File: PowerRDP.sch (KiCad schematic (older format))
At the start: 40 parts, among them J1 Conn_01x02_Male, J10 FPGA, J11 FAA LED, J12 Switch, J2 Conn_01x02_Male, J3 Conn_01x02_Male, J4 Conn_01x02_Male, J5 Conn_01x02_Male, J6 Conn_01x02_Male, J7 3.3V, J8 5V, J9 12V, Q1 NTR4003NT1G, U1 Recom_RS3, U2 LM2575-3.3BU, U3 LM2575-5.0BU, U4 LM2575-12BU, U5 TS555

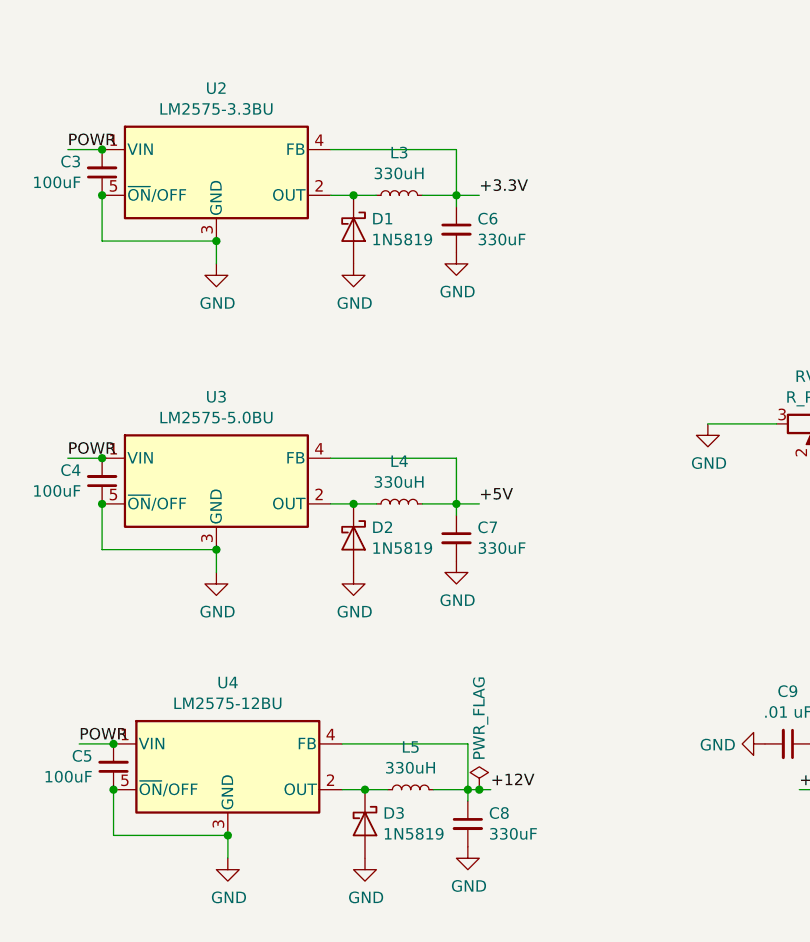
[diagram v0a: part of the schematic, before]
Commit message: Fix capcaitors and inductors and expand board to sustain girth of new components.
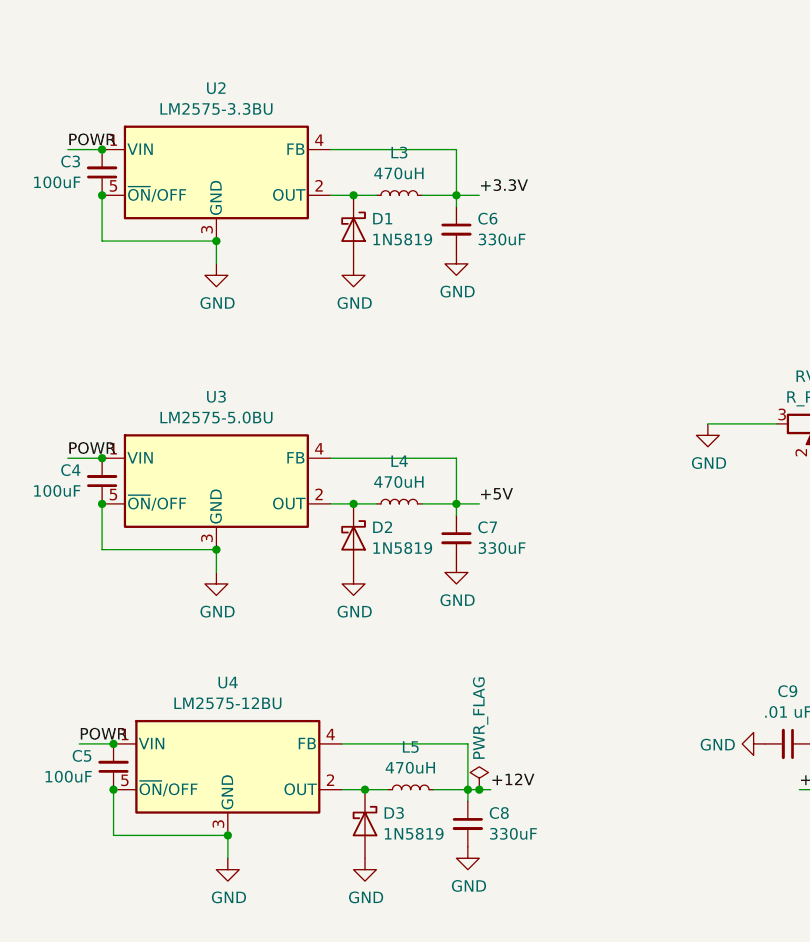
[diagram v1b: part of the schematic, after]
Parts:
- C3, C4, C5: footprint Capacitor_SMD:C_0805_2012Metric_Pad1.15x1.40mm_HandSolder -> Capacitor_SMD:CP_Elec_6.3x7.7
- C6, C7, C8: footprint Capacitor_SMD:C_0805_2012Metric_Pad1.15x1.40mm_HandSolder -> Capacitor_SMD:CP_Elec_8x10
- L3, L4, L5: value 330uH -> 470uH; footprint Inductor_SMD:L_0805_2012Metric_Pad1.15x1.40mm_HandSolder -> Inductor_SMD:L_Bourns_SRR1260
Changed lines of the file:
@@
 P 6850 1350
 F 0 "L3" V 7035 1350 50  0000 C CNN
-F 1 "330uH" V 6944 1350 50  0000 C CNN
-F 2 "Inductor_SMD:L_0805_2012Metric_Pad1.15x1.40mm_HandSolder" H 6850 1350 50  0001 C CNN
+F 1 "470uH" V 6944 1350 50  0000 C CNN
+F 2 "Inductor_SMD:L_Bourns_SRR1260" H 6850 1350 50  0001 C CNN
 F 3 "~" H 6850 1350 50  0001 C CNN
 	1    6850 1350
@@
 F 0 "C6" H 7192 1546 50  0000 L CNN
 F 1 "330uF" H 7192 1455 50  0000 L CNN
-F 2 "Capacitor_SMD:C_0805_2012Metric_Pad1.15x1.40mm_HandSolder" H 7100 1500 50  0001 C CNN
+F 2 "Capacitor_SMD:CP_Elec_8x10" H 7100 1500 50  0001 C CNN
 F 3 "~" H 7100 1500 50  0001 C CNN
 	1    7100 1500
@@
 F 0 "C4" H 5459 2554 50  0000 R CNN
 F 1 "100uF" H 5459 2645 50  0000 R CNN
-F 2 "Capacitor_SMD:C_0805_2012Metric_Pad1.15x1.40mm_HandSolder" H 5550 2600 50  0001 C CNN
+F 2 "Capacitor_SMD:CP_Elec_6.3x7.7" H 5550 2600 50  0001 C CNN
 F 3 "~" H 5550 2600 50  0001 C CNN
 	1    5550 2600
@@
 P 6850 2700
 F 0 "L4" V 7035 2700 50  0000 C CNN
-F 1 "330uH" V 6944 2700 50  0000 C CNN
-F 2 "Inductor_SMD:L_0805_2012Metric_Pad1.15x1.40mm_HandSolder" H 6850 2700 50  0001 C CNN
+F 1 "470uH" V 6944 2700 50  0000 C CNN
+F 2 "Inductor_SMD:L_Bourns_SRR1260" H 6850 2700 50  0001 C CNN
 F 3 "~" H 6850 2700 50  0001 C CNN
 	1    6850 2700
@@
 F 0 "C7" H 7192 2896 50  0000 L CNN
 F 1 "330uF" H 7192 2805 50  0000 L CNN
-F 2 "Capacitor_SMD:C_0805_2012Metric_Pad1.15x1.40mm_HandSolder" H 7100 2850 50  0001 C CNN
+F 2 "Capacitor_SMD:CP_Elec_8x10" H 7100 2850 50  0001 C CNN
 F 3 "~" H 7100 2850 50  0001 C CNN
 	1    7100 2850
@@
 P 6900 3950
 F 0 "L5" V 7085 3950 50  0000 C CNN
-F 1 "330uH" V 6994 3950 50  0000 C CNN
-F 2 "Inductor_SMD:L_0805_2012Metric_Pad1.15x1.40mm_HandSolder" H 6900 3950 50  0001 C CNN
+F 1 "470uH" V 6994 3950 50  0000 C CNN
+F 2 "Inductor_SMD:L_Bourns_SRR1260" H 6900 3950 50  0001 C CNN
 F 3 "~" H 6900 3950 50  0001 C CNN
 	1    6900 3950
@@
 F 0 "C8" H 7242 4146 50  0000 L CNN
 F 1 "330uF" H 7242 4055 50  0000 L CNN
-F 2 "Capacitor_SMD:C_0805_2012Metric_Pad1.15x1.40mm_HandSolder" H 7150 4100 50  0001 C CNN
+F 2 "Capacitor_SMD:CP_Elec_8x10" H 7150 4100 50  0001 C CNN
 F 3 "~" H 7150 4100 50  0001 C CNN
 	1    7150 4100
@@
 F 0 "C3" H 5459 1204 50  0000 R CNN
 F 1 "100uF" H 5459 1295 50  0000 R CNN
-F 2 "Capacitor_SMD:C_0805_2012Metric_Pad1.15x1.40mm_HandSolder" H 5550 1250 50  0001 C CNN
+F 2 "Capacitor_SMD:CP_Elec_6.3x7.7" H 5550 1250 50  0001 C CNN
 F 3 "~" H 5550 1250 50  0001 C CNN
 	1    5550 1250
@@
 F 0 "C5" H 5509 3804 50  0000 R CNN
 F 1 "100uF" H 5509 3895 50  0000 R CNN
-F 2 "Capacitor_SMD:C_0805_2012Metric_Pad1.15x1.40mm_HandSolder" H 5600 3850 50  0001 C CNN
+F 2 "Capacitor_SMD:CP_Elec_6.3x7.7" H 5600 3850 50  0001 C CNN
 F 3 "~" H 5600 3850 50  0001 C CNN
 	1    5600 3850

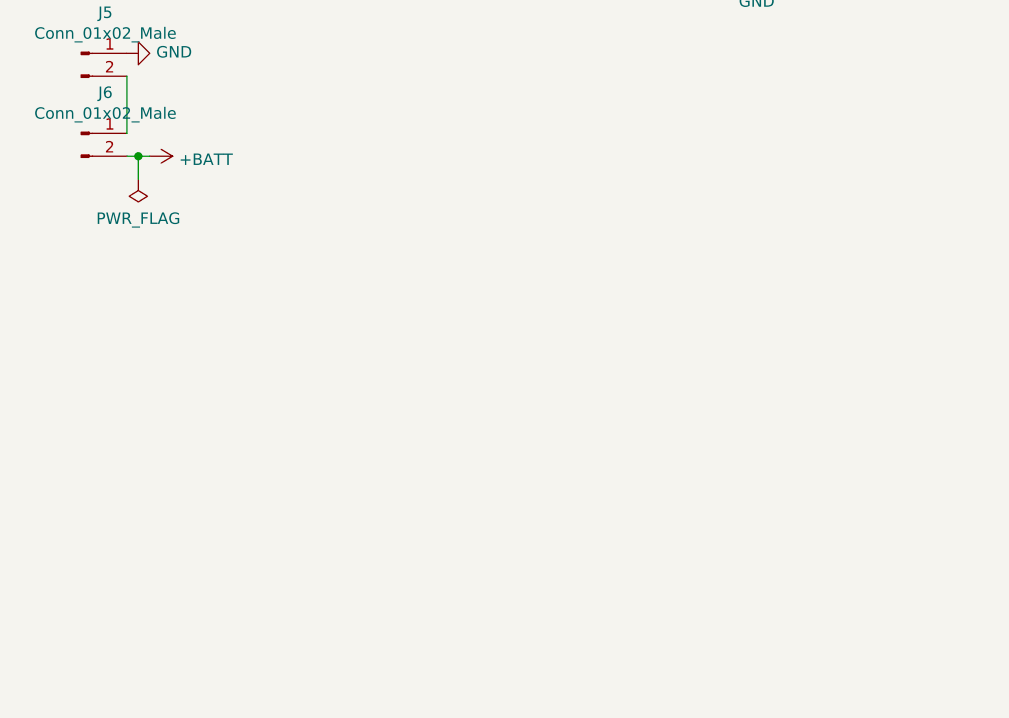
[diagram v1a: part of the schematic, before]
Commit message: Add op amps and SMA connectors for socket voltage reduction
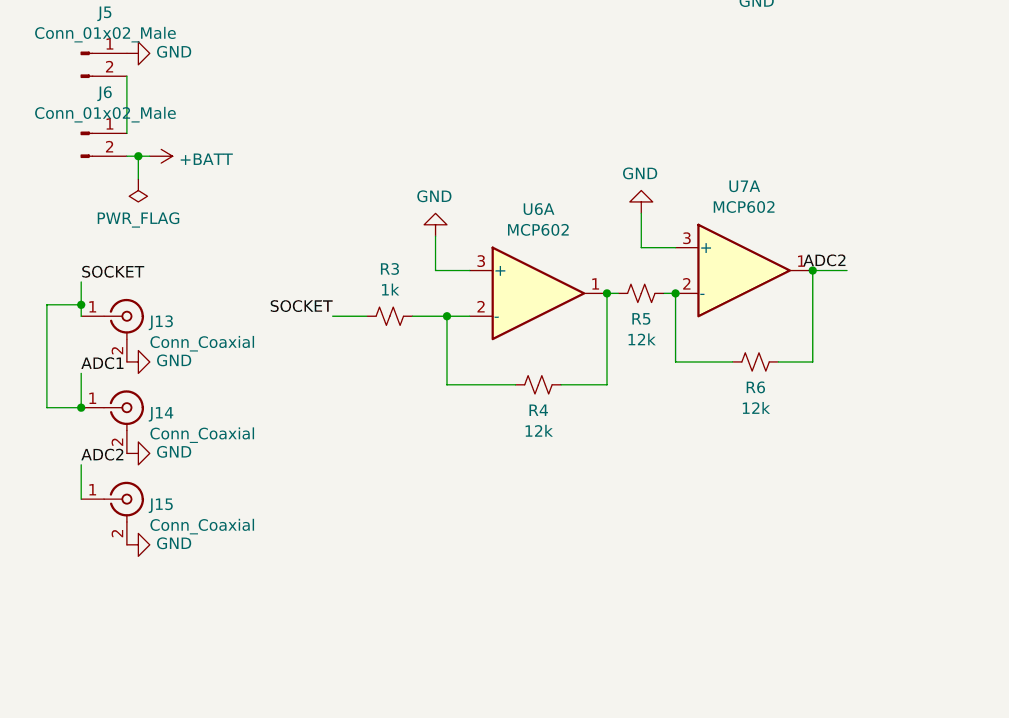
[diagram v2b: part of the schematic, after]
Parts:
- added J13, J14, J15: Conn_Coaxial, Connector_Coaxial:SMA_Amphenol_132134_Vertical, symbol Connector:Conn_Coaxial
- added R3: 1k, Resistor_SMD:R_0805_2012Metric_Pad1.15x1.40mm_HandSolder, symbol Device:R_Small_US
- added R4, R5, R6: 12k, Resistor_SMD:R_0805_2012Metric_Pad1.15x1.40mm_HandSolder, symbol Device:R_Small_US
- added U6, U7: MCP602, Package_SO:SOIC-8_3.9x4.9mm_P1.27mm, symbol Amplifier_Operational:MCP602
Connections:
- net GND: now also J13.2 (Ext), J14.2 (Ext), J15.2 (Ext), U6.3 (+), U7.3 (+)
- new net: R4.1, R5.2, U6.1
- new net: R3.1, R4.2, U6.2 (-)
- new net: R5.1, R6.2, U7.2 (-)
- new net ADC1: J13.1 (In), J14.1 (In), R3.2
- new net ADC2: J15.1 (In), R6.1, U7.1
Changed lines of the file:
@@
 	0    1    1    0
 $EndComp
-Wire Wire Line
-	3300 1150 3500 1150
 $Comp
 L Regulator_Switching:LM2575-3.3BU U2
@@
 NoConn ~ 2850 1750
 NoConn ~ 2750 1750
+$Comp
+L Connector:Conn_Coaxial J13
+U 1 1 5C5A6220
+P 1200 3400
+F 0 "J13" H 1299 3376 50  0000 L CNN
+F 1 "Conn_Coaxial" H 1299 3285 50  0000 L CNN
+F 2 "Connector_Coaxial:SMA_Amphenol_132134_Vertical" H 1200 3400 50  0001 C CNN
+F 3 " ~" H 1200 3400 50  0001 C CNN
+	1    1200 3400
+	1    0    0    -1
+$EndComp
+$Comp
+L Connector:Conn_Coaxial J14
+U 1 1 5C5A65C4
+P 1200 3800
+F 0 "J14" H 1299 3776 50  0000 L CNN
+F 1 "Conn_Coaxial" H 1299 3685 50  0000 L CNN
+F 2 "Connector_Coaxial:SMA_Amphenol_132134_Vertical" H 1200 3800 50  0001 C CNN
+F 3 " ~" H 1200 3800 50  0001 C CNN
+	1    1200 3800
+	1    0    0    -1
+$EndComp
+$Comp
+L Connector:Conn_Coaxial J15
+U 1 1 5C5A663A
+P 1200 4200
+F 0 "J15" H 1299 4176 50  0000 L CNN
+F 1 "Conn_Coaxial" H 1299 4085 50  0000 L CNN
+F 2 "Connector_Coaxial:SMA_Amphenol_132134_Vertical" H 1200 4200 50  0001 C CNN
+F 3 " ~" H 1200 4200 50  0001 C CNN
+	1    1200 4200
+	1    0    0    -1
+$EndComp
+$Comp
+L power:GND #PWR0101
+U 1 1 5C5A6AFF
+P 1200 3600
+F 0 "#PWR0101" H 1200 3350 50  0001 C CNN
+F 1 "GND" V 1205 3472 50  0000 R CNN
+F 2 "" H 1200 3600 50  0001 C CNN
+F 3 "" H 1200 3600 50  0001 C CNN
+	1    1200 3600
+	0    -1   -1   0
+$EndComp
+$Comp
+L power:GND #PWR0102
+U 1 1 5C5A6BE8
+P 1200 4000
+F 0 "#PWR0102" H 1200 3750 50  0001 C CNN
+F 1 "GND" V 1205 3872 50  0000 R CNN
+F 2 "" H 1200 4000 50  0001 C CNN
+F 3 "" H 1200 4000 50  0001 C CNN
+	1    1200 4000
+	0    -1   -1   0
+$EndComp
+$Comp
+L power:GND #PWR0103
+U 1 1 5C5A6C49
+P 1200 4400
+F 0 "#PWR0103" H 1200 4150 50  0001 C CNN
+F 1 "GND" V 1205 4272 50  0000 R CNN
+F 2 "" H 1200 4400 50  0001 C CNN
+F 3 "" H 1200 4400 50  0001 C CNN
+	1    1200 4400
+	0    -1   -1   0
+$EndComp
+Wire Wire Line
+	1000 3400 1000 3350
+Text Label 1000 3250 0    50   ~ 0
+SOCKET
+Wire Wire Line
+	1000 3800 1000 3650
+Wire Wire Line
+	1000 4050 1000 4200
+Text Label 1000 3650 0    50   ~ 0
+ADC1
+Text Label 1000 4050 0    50   ~ 0
+ADC2
+$Comp
+L Amplifier_Operational:MCP602 U6
+U 1 1 5C5B0CBD
+P 3000 3300
+F 0 "U6" H 3000 3667 50  0000 C CNN
+F 1 "MCP602" H 3000 3576 50  0000 C CNN
+F 2 "Package_SO:SOIC-8_3.9x4.9mm_P1.27mm" H 3000 3300 50  0001 C CNN
+F 3 "http://ww1.microchip.com/downloads/en/DeviceDoc/21314g.pdf" H 3000 3300 50  0001 C CNN
+	1    3000 3300
+	1    0    0    -1
+$EndComp
+$Comp
+L Amplifier_Operational:MCP602 U7
+U 1 1 5C5B1155
+P 3900 3200
+F 0 "U7" H 3900 3567 50  0000 C CNN
+F 1 "MCP602" H 3900 3476 50  0000 C CNN
+F 2 "Package_SO:SOIC-8_3.9x4.9mm_P1.27mm" H 3900 3200 50  0001 C CNN
+F 3 "http://ww1.microchip.com/downloads/en/DeviceDoc/21314g.pdf" H 3900 3200 50  0001 C CNN
+	1    3900 3200
+	1    0    0    -1
+$EndComp
+$Comp
+L Device:R_Small_US R4
+U 1 1 5C5B184F
+P 3000 3700
+F 0 "R4" V 3113 3700 50  0000 C CNN
+F 1 "12k" V 3204 3700 50  0000 C CNN
+F 2 "Resistor_SMD:R_0805_2012Metric_Pad1.15x1.40mm_HandSolder" H 3000 3700 50  0001 C CNN
+F 3 "~" H 3000 3700 50  0001 C CNN
+	1    3000 3700
+	0    1    1    0
+$EndComp
+$Comp
+L Device:R_Small_US R3
+U 1 1 5C5B1902
+P 2350 3400
+F 0 "R3" V 2145 3400 50  0000 C CNN
+F 1 "1k" V 2236 3400 50  0000 C CNN
+F 2 "Resistor_SMD:R_0805_2012Metric_Pad1.15x1.40mm_HandSolder" H 2350 3400 50  0001 C CNN
+F 3 "~" H 2350 3400 50  0001 C CNN
+	1    2350 3400
+	0    1    1    0
+$EndComp
+Wire Wire Line
+	2700 3200 2550 3200
+Wire Wire Line
+	2550 3200 2550 3050
+$Comp
+L power:GND #PWR0104
+U 1 1 5C5B40F0
+P 2550 3050
+F 0 "#PWR0104" H 2550 2800 50  0001 C CNN
+F 1 "GND" H 2555 2877 50  0000 C CNN
+F 2 "" H 2550 3050 50  0001 C CNN
+F 3 "" H 2550 3050 50  0001 C CNN
+	1    2550 3050
+	-1   0    0    1
+$EndComp
+Wire Wire Line
+	3600 3100 3450 3100
+Wire Wire Line
+	3450 3100 3450 2950
+$Comp
+L power:GND #PWR0105
+U 1 1 5C5B6C86
+P 3450 2950
+F 0 "#PWR0105" H 3450 2700 50  0001 C CNN
+F 1 "GND" H 3455 2777 50  0000 C CNN
+F 2 "" H 3450 2950 50  0001 C CNN
+F 3 "" H 3450 2950 50  0001 C CNN
+	1    3450 2950
+	-1   0    0    1
+$EndComp
+Wire Wire Line
+	2100 3400 2250 3400
+Wire Wire Line
+	2450 3400 2600 3400
+Wire Wire Line
+	2600 3400 2600 3700
+Wire Wire Line
+	2600 3700 2900 3700
+Connection ~ 2600 3400
+Wire Wire Line
+	2600 3400 2700 3400
+$Comp
+L Device:R_Small_US R5
+U 1 1 5C5C27B8
+P 3450 3300
+F 0 "R5" V 3563 3300 50  0000 C CNN
+F 1 "12k" V 3654 3300 50  0000 C CNN
+F 2 "Resistor_SMD:R_0805_2012Metric_Pad1.15x1.40mm_HandSolder" H 3450 3300 50  0001 C CNN
+F 3 "~" H 3450 3300 50  0001 C CNN
+	1    3450 3300
+	0    1    1    0
+$EndComp
+Wire Wire Line
+	3100 3700 3300 3700
+Wire Wire Line
+	3300 3700 3300 3300
+Wire Wire Line
+	3350 3300 3300 3300
+Connection ~ 3300 3300
+Wire Wire Line
+	3550 3300 3600 3300
+$Comp
+L Device:R_Small_US R6
+U 1 1 5C5CC379
+P 3950 3600
+F 0 "R6" V 4063 3600 50  0000 C CNN
+F 1 "12k" V 4154 3600 50  0000 C CNN
+F 2 "Resistor_SMD:R_0805_2012Metric_Pad1.15x1.40mm_HandSolder" H 3950 3600 50  0001 C CNN
+F 3 "~" H 3950 3600 50  0001 C CNN
+	1    3950 3600
+	0    1    1    0
+$EndComp
+Wire Wire Line
+	3600 3300 3600 3600
+Wire Wire Line
+	3600 3600 3850 3600
+Connection ~ 3600 3300
+Wire Wire Line
+	4050 3600 4200 3600
+Wire Wire Line
+	4200 3600 4200 3200
+Wire Wire Line
+	4200 3200 4350 3200
+Connection ~ 4200 3200
+Text Label 4350 3200 2    50   ~ 0
+ADC2
+Wire Wire Line
+	1000 3350 850  3350
+Wire Wire Line
+	850  3350 850  3800
+Wire Wire Line
+	850  3800 1000 3800
+Connection ~ 1000 3350
+Wire Wire Line
+	1000 3350 1000 3250
+Connection ~ 1000 3800
+Text Label 2100 3400 2    50   ~ 0
+SOCKET
+Wire Wire Line
+	3300 1150 3500 1150
 $EndSCHEMATC

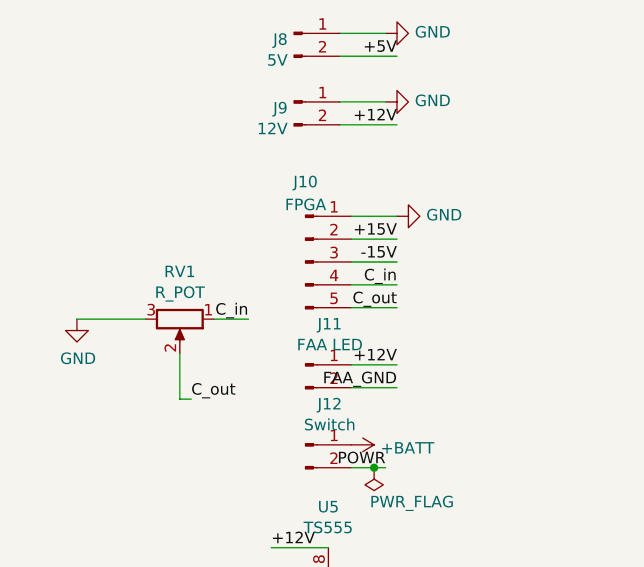
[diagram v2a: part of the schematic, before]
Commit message: Change R3 to through-hole for easier changes of amplification
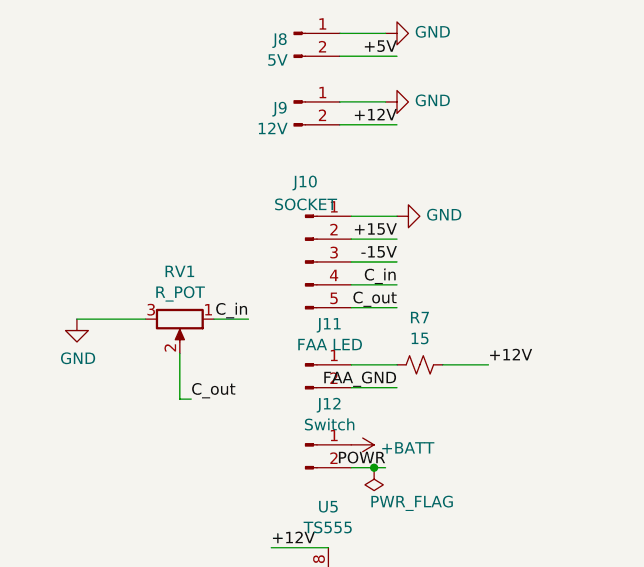
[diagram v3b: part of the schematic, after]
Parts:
- added R7: 15, Resistor_SMD:R_0805_2012Metric_Pad1.15x1.40mm_HandSolder, symbol Device:R_Small_US
- J10: value FPGA -> SOCKET
- R3: footprint Resistor_SMD:R_0805_2012Metric_Pad1.15x1.40mm_HandSolder -> Resistor_THT:R_Axial_DIN0204_L3.6mm_D1.6mm_P5.08mm_Horizontal
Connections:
- net +12V: now also R7.1; no longer J11.1 (Pin_1)
- new net: J11.1 (Pin_1), R7.2
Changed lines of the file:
@@
 P 9200 2100
 F 0 "J10" H 9200 2450 50  0000 C CNN
-F 1 "FPGA" H 9200 2350 50  0000 C CNN
+F 1 "SOCKET" H 9200 2350 50  0000 C CNN
 F 2 "Connector_Molex:Molex_KK-254_AE-6410-05A_1x05_P2.54mm_Vertical" H 9200 2100 50  0001 C CNN
 F 3 "~" H 9200 2100 50  0001 C CNN
@@
 Text Label 9600 4750 0    50   ~ 0
 FAA_GND
-Text Label 9600 2550 2    50   ~ 0
-+12V
 $Comp
 L Connector:Conn_01x02_Male J12
@@
 F 0 "R3" V 2145 3400 50  0000 C CNN
 F 1 "1k" V 2236 3400 50  0000 C CNN
-F 2 "Resistor_SMD:R_0805_2012Metric_Pad1.15x1.40mm_HandSolder" H 2350 3400 50  0001 C CNN
+F 2 "Resistor_THT:R_Axial_DIN0204_L3.6mm_D1.6mm_P5.08mm_Horizontal" H 2350 3400 50  0001 C CNN
 F 3 "~" H 2350 3400 50  0001 C CNN
 	1    2350 3400
@@
 Wire Wire Line
 	3300 1150 3500 1150
+$Comp
+L Device:R_Small_US R7
+U 1 1 5C68726B
+P 9700 2550
+F 0 "R7" V 9495 2550 50  0000 C CNN
+F 1 "15" V 9586 2550 50  0000 C CNN
+F 2 "Resistor_SMD:R_0805_2012Metric_Pad1.15x1.40mm_HandSolder" H 9700 2550 50  0001 C CNN
+F 3 "~" H 9700 2550 50  0001 C CNN
+	1    9700 2550
+	0    1    1    0
+$EndComp
+Wire Wire Line
+	9800 2550 10000 2550
+Text Label 10000 2550 0    50   ~ 0
++12V
 $EndSCHEMATC

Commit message: Fix opamps
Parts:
- U6, U7: symbol Amplifier_Operational:MCP602 -> Amplifier_Operational:LM741
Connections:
- net +3.3V: now also U6.7 (V+), U7.7 (V+)
- net ADC2: now also U7.6; no longer U7.1
- net GND: now also U6.4 (V-), U7.4 (V-)
- net at R4.1, R5.2: now also U6.6; no longer U6.1
- no-connect marks 3 -> 7
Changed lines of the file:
@@
 ADC2
 $Comp
-L Amplifier_Operational:MCP602 U6
+L Amplifier_Operational:LM741 U6
 U 1 1 5C5B0CBD
 P 3000 3300
@@
 $EndComp
 $Comp
-L Amplifier_Operational:MCP602 U7
+L Amplifier_Operational:LM741 U7
 U 1 1 5C5B1155
 P 3900 3200
-F 0 "U7" H 3900 3567 50  0000 C CNN
-F 1 "MCP602" H 3900 3476 50  0000 C CNN
+F 0 "U7" H 4241 3246 50  0000 L CNN
+F 1 "MCP602" H 4241 3155 50  0000 L CNN
 F 2 "Package_SO:SOIC-8_3.9x4.9mm_P1.27mm" H 3900 3200 50  0001 C CNN
 F 3 "http://ww1.microchip.com/downloads/en/DeviceDoc/21314g.pdf" H 3900 3200 50  0001 C CNN
@@
 Text Label 10000 2550 0    50   ~ 0
 +12V
+Wire Wire Line
+	3800 2750 3800 2900
+Text Label 2900 2900 0    50   ~ 0
++3.3V
+Text Label 3800 2750 0    50   ~ 0
++3.3V
+$Comp
+L power:GND #PWR0106
+U 1 1 5C712204
+P 2900 3600
+F 0 "#PWR0106" H 2900 3350 50  0001 C CNN
+F 1 "GND" V 2905 3472 50  0000 R CNN
+F 2 "" H 2900 3600 50  0001 C CNN
+F 3 "" H 2900 3600 50  0001 C CNN
+	1    2900 3600
+	0    1    1    0
+$EndComp
+$Comp
+L power:GND #PWR0107
+U 1 1 5C7122EE
+P 3800 3500
+F 0 "#PWR0107" H 3800 3250 50  0001 C CNN
+F 1 "GND" V 3805 3372 50  0000 R CNN
+F 2 "" H 3800 3500 50  0001 C CNN
+F 3 "" H 3800 3500 50  0001 C CNN
+	1    3800 3500
+	0    1    1    0
+$EndComp
+NoConn ~ 3000 3600
+NoConn ~ 3100 3600
+NoConn ~ 3900 3500
+NoConn ~ 4000 3500
+Wire Wire Line
+	2900 2900 2900 3000
 $EndSCHEMATC
